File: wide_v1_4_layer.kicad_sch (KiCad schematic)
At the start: 14 parts

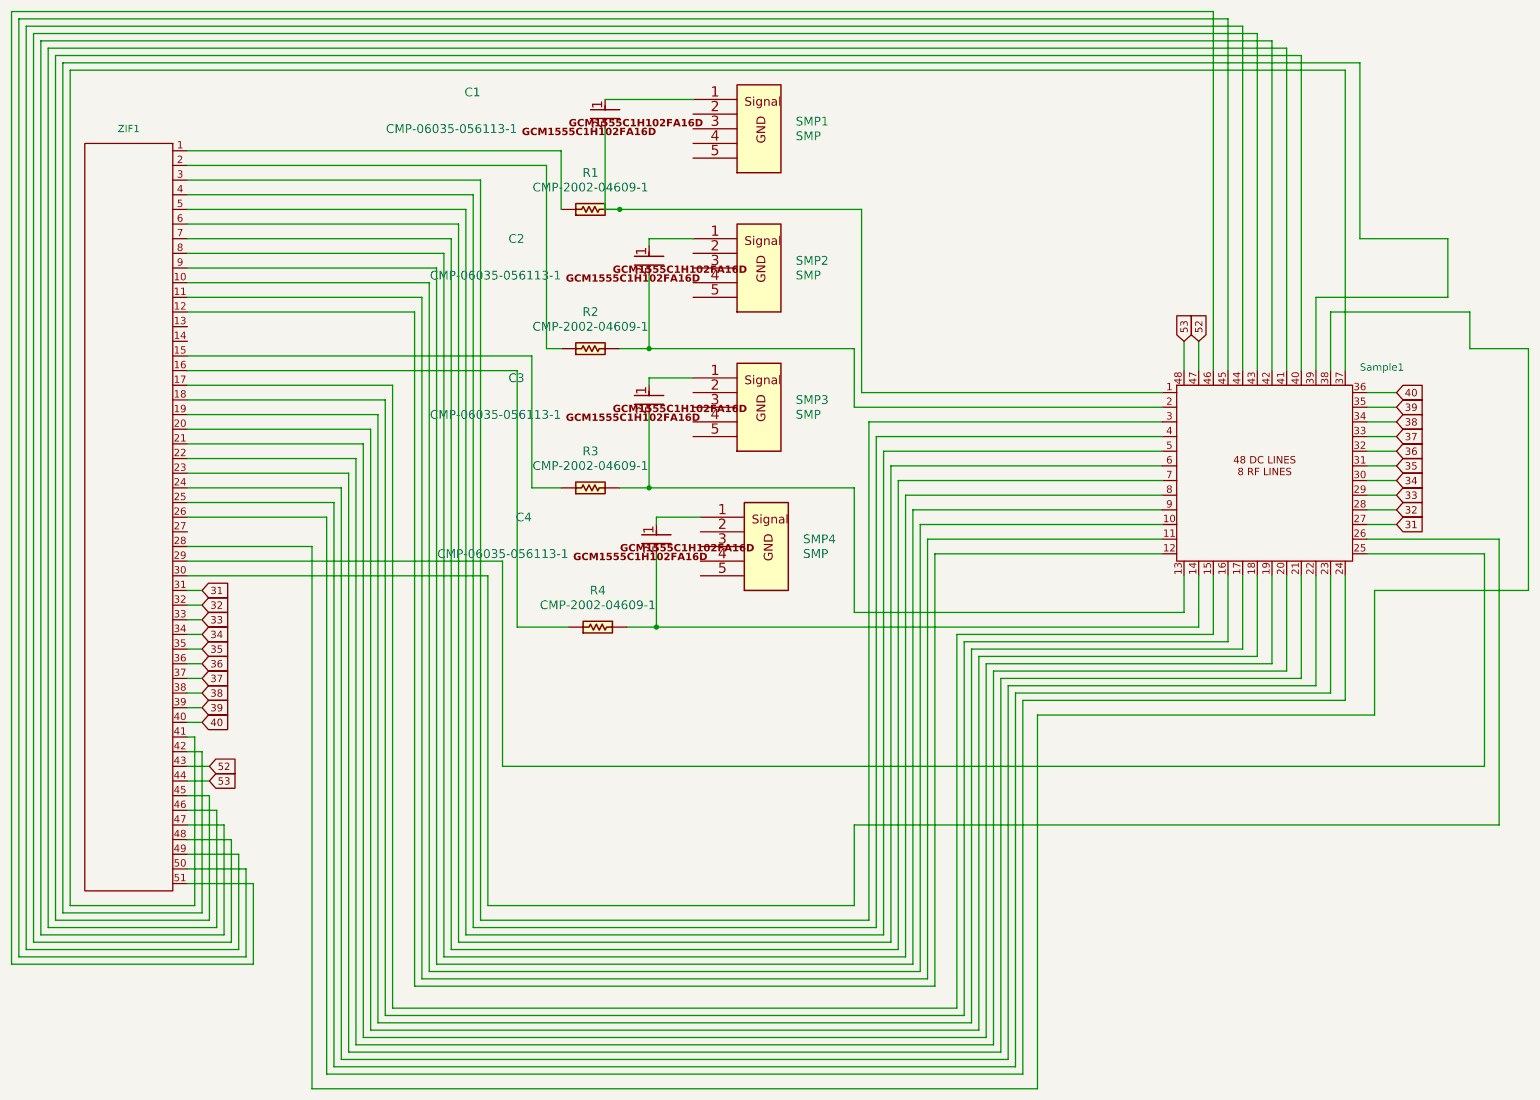
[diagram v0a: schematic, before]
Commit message: redoing PCB with updated layers
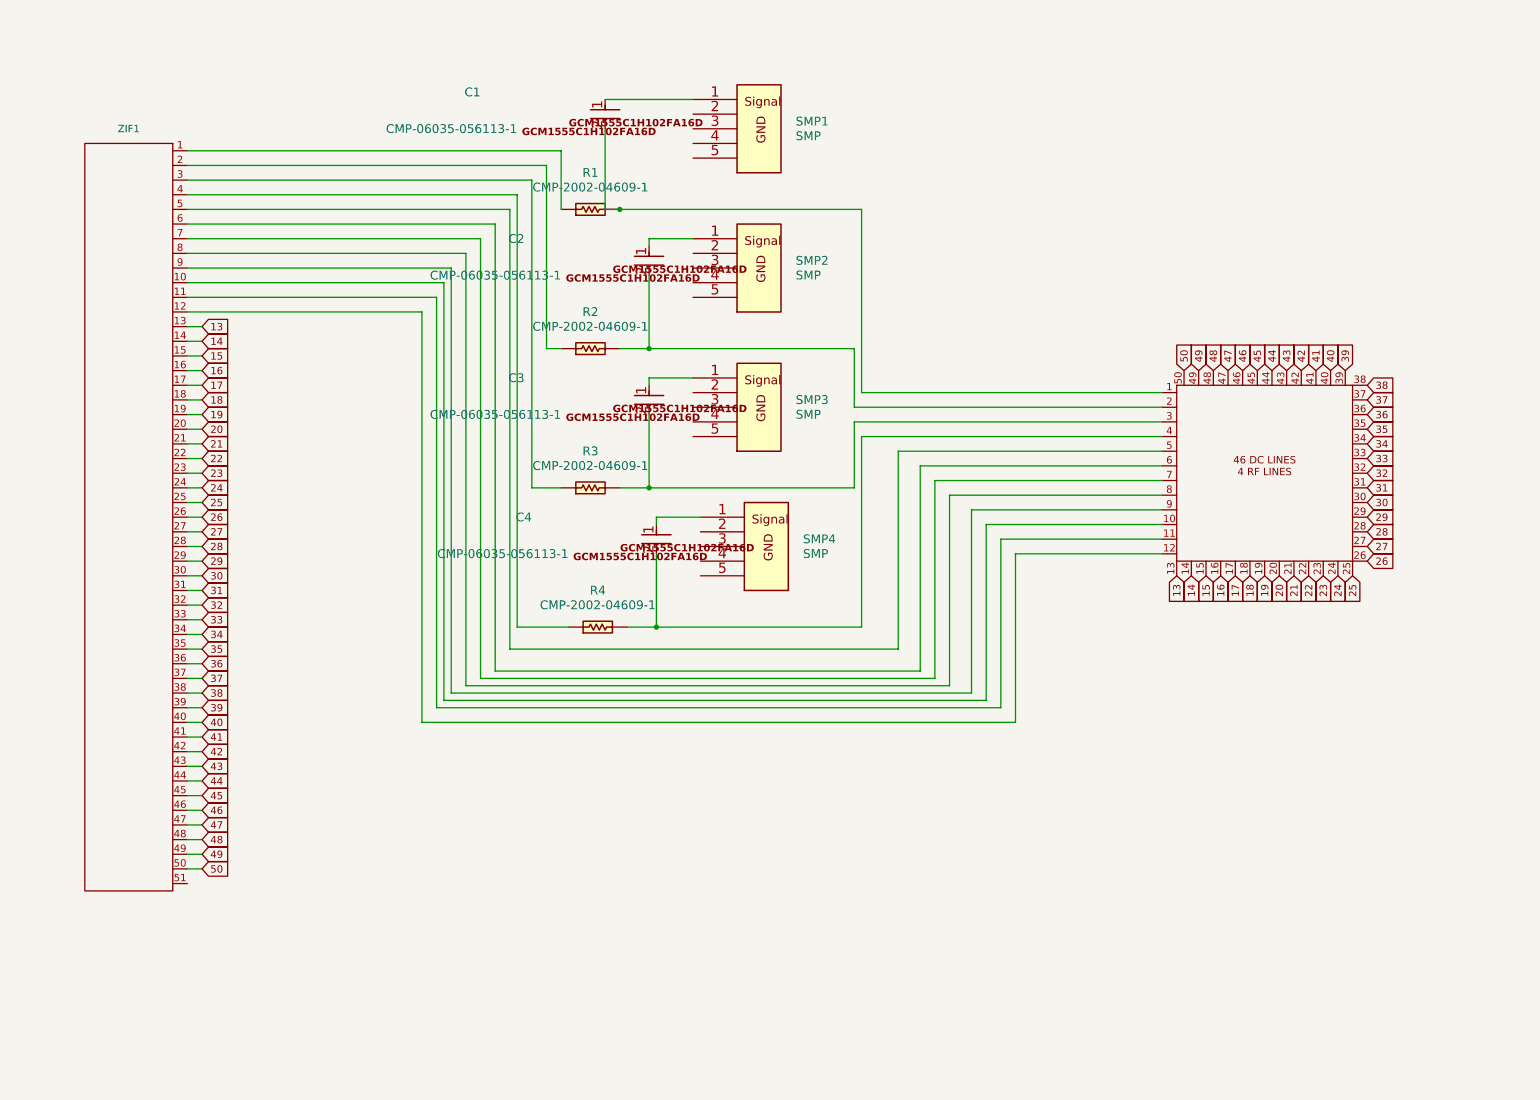
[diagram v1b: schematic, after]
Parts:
- C1, C2, C3, C4: footprint PcbLib_narrow_v2:CAPC1005X06N -> Capacitor_SMD:C_0402_1005Metric
- R1: footprint PcbLib_narrow_v2:RESC1005X04N -> Capacitor_SMD:C_0402_1005Metric
- R2, R3, R4: footprint PcbLib_narrow_v2:RESC1005X04N -> Resistor_SMD:R_0402_1005Metric
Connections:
- net 31: now also Sample1.31; no longer Sample1.27
- net 32: now also Sample1.32; no longer Sample1.28
- net 33: now also Sample1.33; no longer Sample1.29
- net 34: now also Sample1.34; no longer Sample1.30
- net 35: now also Sample1.35; no longer Sample1.31
- net 36: now also Sample1.36; no longer Sample1.32
- net 37: now also Sample1.37; no longer Sample1.33
- net 38: now also Sample1.38; no longer Sample1.34
- net 39: now also Sample1.39; no longer Sample1.35
- net 40: now also Sample1.40; no longer Sample1.36
- net at C3.2, R3.2: now also Sample1.3; no longer Sample1.13
- net at R3.1: now also ZIF1.3; no longer ZIF1.15
- net at R4.1: now also ZIF1.4; no longer ZIF1.16
- net at C4.2, R4.2: now also Sample1.4; no longer Sample1.14
- net 13: now reaches ZIF1.13
- net 13: now also Sample1.13
- net 14: now reaches ZIF1.14
- net 14: now also Sample1.14
- net 15: now reaches Sample1.15
- net 15: now also ZIF1.15; no longer ZIF1.17
- net 16: now reaches Sample1.16
- net 16: now also ZIF1.16; no longer ZIF1.18
- net 17: now reaches Sample1.17
- net 17: now also ZIF1.17; no longer ZIF1.19
- net 18: now reaches Sample1.18
- net 18: now also ZIF1.18; no longer ZIF1.20
- net 19: now reaches Sample1.19
- net 19: now also ZIF1.19; no longer ZIF1.21
- net 20: now reaches Sample1.20
- net 20: now also ZIF1.20; no longer ZIF1.22
- net 21: now reaches Sample1.21
- net 21: now also ZIF1.21; no longer ZIF1.23
- net 22: now reaches Sample1.22
- net 22: now also ZIF1.22; no longer ZIF1.24
- net 23: now reaches Sample1.23
- net 23: now also ZIF1.23; no longer ZIF1.25
- net 24: now reaches Sample1.24
- net 24: now also ZIF1.24; no longer ZIF1.26
- net 27: now reaches ZIF1.27
- net 27: now also Sample1.27
- net 28: now reaches ZIF1.28
- net 28: now also Sample1.28; no longer Sample1.38
- net 25: now reaches Sample1.25
- net 25: now also ZIF1.25; no longer ZIF1.29
- net 26: now reaches Sample1.26
- net 26: now also ZIF1.26; no longer ZIF1.30
- net 41: now reaches ZIF1.41
- net 41: now also Sample1.41; no longer Sample1.37
- net 42: now reaches ZIF1.42
- net 42: now also Sample1.42; no longer Sample1.39
- net 45: now reaches ZIF1.45
- net 45: now also Sample1.45; no longer Sample1.40
- net 46: now reaches ZIF1.46
- net 46: now also Sample1.46; no longer Sample1.41
- net 47: now reaches ZIF1.47
- net 47: now also Sample1.47; no longer Sample1.42
- net 43: now reaches Sample1.43
- net 43: now also ZIF1.43; no longer ZIF1.48
- net 44: now reaches Sample1.44
- net 44: now also ZIF1.44; no longer ZIF1.49
- net 50: now reaches ZIF1.50
- net 50: now also Sample1.50; no longer Sample1.45
- net at ZIF1.51: no longer Sample1.46
- removed net 52: Sample1.47, ZIF1.43
- net 53 renamed 48
- net 48: now also ZIF1.48; no longer ZIF1.44
- new net 29: Sample1.29, ZIF1.29
- new net 30: Sample1.30, ZIF1.30
- new net 49: Sample1.49, ZIF1.49
